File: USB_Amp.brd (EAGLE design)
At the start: 87 x 60 mm, 192 parts, among them CON1 AUDIO_IN, CON2 PROG, CON3 PWR IN, CON4 USB-C-2OZ, CON5 SWD, IC1 ISO7762, IC10 74LVC1G79, IC11 1.8V, IC12 AK1110, IC13 STM32G030F, IC14 CH221, IC15 7808, IC16 TAR5SB33, IC2 3.3V, IC3 PIC32MZEF, IC4 TAR5SB33, IC5 SSM3582, IC6 3G04, IC7 TL431, IC8 74LVC1G79, IC9 74LVC1G79, Q1 PNP, Q2 PNP, Q3 PNP, Q4 NPN, Q5 NPN, X1 12MHz, X2 22.5792MHz, X3 24.576MHz

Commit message: 微修正
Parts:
- added TP19, TP20: L_P, my_connector:TESTPIN-MID
- added TP21, TP22: R_N, my_connector:TESTPIN-MID
- L1, L2: value 7uH -> 7uH-UA8013
- R20: value LRCLK -> DATA
- R21: value DATA -> LRCLK
- moved C17 1.00 mm to (29.0, 25.4)
- moved C18 1.00 mm to (29.0, 34.6)
- moved C21 1.00 mm to (21.0, 25.4)
- moved C22 1.00 mm to (21.0, 34.6)
- moved C25 1.00 mm to (27.0, 23.8)
- moved C26 1.00 mm to (23.0, 23.8)
- moved C27 1.00 mm to (18.5, 29.0)
- moved C28 1.00 mm to (18.5, 31.0)
- moved C29 1.00 mm to (23.0, 36.2)
- moved C30 1.00 mm to (27.0, 36.2)
- moved C33 1.00 mm to (23.0, 37.5)
- moved C34 1.00 mm to (23.0, 22.5)
- moved C36 1.00 mm to (27.0, 37.5)
- moved C37 1.00 mm to (27.0, 22.5)
- moved C39 1.00 mm to (25.0, 22.0)
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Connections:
- net SPK_OUTN_L: now also TP19.1
- net SPK_OUTN_R: now also TP22.1
- net SPK_OUTP_L: now also TP20.1
- net SPK_OUTP_R: now also TP21.1
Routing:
- net GND: track 103.3 -> 98.6 mm, vias 773 -> 777
- net I2S_SCK_BUF: track 19.0 -> 20.0 mm
- net I2S_LRCLK_BUF: track 19.2 -> 20.2 mm
- net I2S_DATA_BUF: track 18.9 -> 19.9 mm
- net I2C_SDA: track 56.8 -> 57.8 mm
- net I2C_SCL: track 60.2 -> 61.2 mm
- net +8V: track 101.8 -> 102.8 mm
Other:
- board size 87 x 60 mm -> 88 x 60.1 mm

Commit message: v4.3
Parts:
- added D5, D6, D7, D8: SBD, my_rcl:SOD323
- added R42, R43: THJ, my_rcl:3216-2
- moved C46 1.03 mm to (35.0, 37.5)
- moved C47 1.03 mm to (35.0, 22.5)
- moved C1 1.00 mm to (84.2, 8.50)
- moved C10 1.00 mm to (65.8, 11.5)
- moved C11 1.00 mm to (65.8, 9.00)
- moved C12 1.00 mm to (74.2, 11.0)
- moved C13 1.00 mm to (71.5, 6.25)
- moved C14 1.00 mm to (78.5, 10.0)
- moved C15 1.00 mm to (77.8, 15.5)
- moved C16 1.00 mm to (52.5, 12.2)
- moved C17 1.00 mm to (30.0, 25.4)
- moved C18 1.00 mm to (30.0, 34.6)
- moved C19 1.00 mm to (57.2, 15.8)
- moved C2 1.00 mm to (82.0, 8.50)
- moved C20 1.00 mm to (51.2, 15.8)
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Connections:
- net AMP_OUTN_L: now also D5.2
- net AMP_OUTN_R: now also D8.2
- net AMP_OUTP_L: now also D6.2
- net AMP_OUTP_R: now also D7.2
- net DGND: now also R42.1, R43.1
- net GND: now also D5.1, D6.1, D7.1, D8.1, R42.2, R43.2
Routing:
- net GND: track 98.6 -> 95.0 mm, vias 777 -> 791
- net DGND: track 7.65 -> 9.61 mm, vias 112 -> 113
- net AMP_+5V: track 18.8 -> 19.9 mm
- added copper zone on layer 2, net GND4
- added copper zone on layer 1, net GND5
- added copper zone on layer 15, net GND5
- added copper zone on layer 16, net GND5
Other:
- board size 88 x 60.1 mm -> 88 x 60 mm
- board text added: "ver4.3"
- board text removed: "ver4.2"

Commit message: v6
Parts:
- removed D5, D6, D7, D8: SBD, my_rcl:SOD323
- removed FB6: FB, my_rcl:3216-FB
- added C89: 10n, my_rcl:3216
- added C90, C91: 0.1u, my_rcl:1005
- added IC17: 3.3V, my_ic:SOT23-5
- added R44: 1.5k, my_rcl:1608
- added R45, R46: THJ, my_rcl:1608-W
- added TP23: SDOUT, my_connector:TESTPAD-SMALL
- added TP24: G, my_connector:TESTPIN
- C1, C5: device my_rcl:2012 -> my_rcl:2012-POL
- C12: value 0.1u -> 2.2u; device my_rcl:1608C -> my_rcl:2012
- C13: value 1u -> 0.1u
- C14, C15: value 10p -> 0.1u; device my_rcl:1005 -> my_rcl:1608C
- C16: value 10u -> 0.1u; device my_rcl:2012-POL -> my_rcl:1608C
- C17, C18: value 0.22u -> 0.1u
- C19: value 2.2u -> 0.1u; device my_rcl:2012-POL -> my_rcl:1608C
- C2: value 1u -> 10u; device my_rcl:1608C -> my_rcl:2012
- C20: value 10u -> 0.1u; device my_rcl:2012-POL -> my_rcl:1005
- C21: value 0.22u -> 1u
- C22: value 0.22u -> 0.1u; device my_rcl:1608C -> my_rcl:1005
- C23: value 10u -> 1u; device my_rcl:2012 -> my_rcl:1005
- C24: value 2.2u -> 0.1u; device my_rcl:2012 -> my_rcl:1005
- C25, C26: value 10n -> 10p
- C27, C28, C7: device my_rcl:1608C -> my_rcl:1005
- C29: value 10n -> 1u; device my_rcl:1005 -> my_rcl:2012
- C3: value 0.1u -> 1u
- C30: value 10n -> 1u; device my_rcl:1005 -> my_rcl:1608C
- C31: value 0.1u -> 1u; device my_rcl:1608C -> my_rcl:2012
- C32: value 0.1u -> 0.47u
- C33: value 0.1u -> 1u; device my_rcl:1005 -> my_rcl:1608C
- C34, C35: value 0.1u -> 10u; device my_rcl:1005 -> my_rcl:3225
- C36: value 0.1u -> 0.47u; device my_rcl:1005 -> my_rcl:1608C
- C37: device my_rcl:1005 -> my_rcl:1608C
- C38: value 0.1u -> 25V 1000u; device my_rcl:1005 -> my_rcl:E5-10
- C39: value 1u -> 25V 1000u; device my_rcl:2012 -> my_rcl:E5-10
- C4: value 0.1u -> 2.2u; device my_rcl:1005 -> my_rcl:2012-POL
- C40: device my_rcl:2012 -> my_rcl:1608-W
- C42: value DNP -> 1u; device my_rcl:1608C -> my_rcl:3216-POL
- C43, C44: value 10u -> 0.1u; device my_rcl:3225 -> my_rcl:1005
- C45: value 0.1u -> 1u; device my_rcl:1005 -> my_rcl:2012
- C46: value 10u -> 1u; device my_rcl:3225 -> my_rcl:1608C
- C47: value 10u -> 1u; device my_rcl:3225 -> my_rcl:2012
- C48: value 4.7u -> 0.47u; device my_rcl:3216 -> my_rcl:1608C
- C49: value 16V 680u -> 1u; device my_rcl:E5-10 -> my_rcl:1608C
- C50: value 16V 680u -> 10u; device my_rcl:E5-10 -> my_rcl:3225
- C51: value 100p -> 1u
- C52: value 0.22u -> 10u; device my_rcl:C050W -> my_rcl:3225
- C53: value 100p -> 0.1u
- C54: value 16V 2200u -> 0.47u; device my_rcl:E5-13 -> my_rcl:1608C
- C55: value 1n -> 10u; device my_rcl:2012 -> my_rcl:3216
- C56: value 1n -> 1u; device my_rcl:2012 -> my_rcl:1608-W
- C57: value 10n -> 0.1u; device my_rcl:C050W2 -> my_rcl:1005
- C58: value 10n -> 1u; device my_rcl:C050W2 -> my_rcl:3216-POL
- C59: value 47u -> 0.1u; device my_rcl:E2.5-5 -> my_rcl:1608C
- C60: value 10u -> 100p; device my_rcl:2012 -> my_rcl:1608C
- C61: value 4.7u -> 100p; device my_rcl:2012 -> my_rcl:1608C
- C62: value 100u -> 22u; device my_rcl:E2.5-6.5 -> my_rcl:2012
- C63: value 0.1u -> DNP
- C65: value 0.22u -> 100p; device my_rcl:C050W -> my_rcl:1608C
- C66: value 100p -> 0.47u; device my_rcl:1608C -> my_rcl:C050W
- C67: value 1n -> 0.47u; device my_rcl:2012 -> my_rcl:C050W
- C68: value 1n -> 4.7u; device my_rcl:2012 -> my_rcl:3216
- C69: value 10u -> 1n
- C70: value 10n -> 1n; device my_rcl:C050W2 -> my_rcl:2012
- C71: value 10n -> 16V 680u; device my_rcl:C050W2 -> my_rcl:E5-10
- C72, C73: value 10u -> 10n; device my_rcl:2012 -> my_rcl:3216
- C74: value 0.1u -> 16V 680u; device my_rcl:1608C -> my_rcl:E5-10
- C76: value 25V 1000u -> 16V 2200u; device my_rcl:E5-10 -> my_rcl:E5-13
- C78: value 25V 1000u -> 100p; device my_rcl:E5-10 -> my_rcl:1608C
- C79: value 1u -> 100p
- C8, C9: value 0.1u -> 10u; device my_rcl:1608C -> my_rcl:2012
- C80: value 0.1u -> 100p
- C81: value 10u -> 100p; device my_rcl:3216 -> my_rcl:1608C
- C82: value 0.1u -> 0.47u; device my_rcl:1608C -> my_rcl:C050W
- C83: value 22u -> 0.47u; device my_rcl:2012 -> my_rcl:C050W
- C84: value 4.7u -> 10u
- C85: value 100p -> 10u; device my_rcl:1608C -> my_rcl:2012
- C86, C87: value 100p -> 1n; device my_rcl:1608C -> my_rcl:2012
- C88: value 100p -> 10n; device my_rcl:1608C -> my_rcl:3216
- FB4: device my_rcl:2012-R -> my_rcl:3216-FB
- IC1: value ISO7762 -> TAR5SB33; device my_ic:TSSOP16 -> my_ic:SOT23-5
- IC10: value 74LVC1G79 -> CH221; device my_ic:TSSOP5 -> my_ic:SOT23-6
- IC11: value 1.8V -> TAS5827; device my_ic:SOT23-5 -> my_ic:QFN32-TAS
- IC12: value AK1110 -> 7805; device my_ic:PLP10 -> my_ic:DPAK
- IC13: value STM32G030F -> TAR5SB33; device my_ic:TSSOP20 -> my_ic:SOT23-5
- IC14: value CH221 -> TL431; device my_ic:SOT23-6 -> my_ic:SC59
- IC15: value 7808 -> STM32G030F; device my_ic:DPAK -> my_ic:TSSOP20
- IC16: value TAR5SB33 -> 3.3V
- IC2: value 3.3V -> ISO7762; device my_ic:SOT23-5 -> my_ic:TSSOP16
- IC3: value PIC32MZEF -> 3.3V; device my_ic:QFN64HT -> my_ic:SOT23-5
- IC4: value TAR5SB33 -> 3G04; device my_ic:SOT23-5 -> my_ic:SSOP8-P-0.65
- IC5: value SSM3582 -> PIC32MZEF; device my_ic:QFN40HT -> my_ic:QFN64HT
- IC6: value 3G04 -> 74LVC1G79; device my_ic:SSOP8-P-0.65 -> my_ic:TSSOP5
- IC7: value TL431 -> 74LVC1G79; device my_ic:SC59 -> my_ic:TSSOP5
- IC9: value 74LVC1G79 -> TAS5827; device my_ic:TSSOP5 -> my_ic:QFN32-TAS
- R11: value 51 -> MCLK
- R12: value 39.2k -> MCLKB; device my_rcl:1608 -> my_rcl:1005
- R13: value 10k -> DATA; device my_rcl:1608 -> my_rcl:1005
- R14: value 1k -> LRCLK; device my_rcl:3216 -> my_rcl:1005
- R15: value 51 -> SCK; device my_rcl:2012 -> my_rcl:1005
- R16: value 51 -> 0; device my_rcl:2012 -> my_rcl:1005
- R17: value MCLK -> 5.1k; device my_rcl:1005 -> my_rcl:1608
- R18: value MCLKB -> 5.1k; device my_rcl:1005 -> my_rcl:1608
- R19: value SCK -> 200k; device my_rcl:1005 -> my_rcl:1608
- R20: value DATA -> 1k
- R21: value LRCLK -> 1k; device my_rcl:1005 -> my_rcl:2012
- R22: value 2.2 -> 100; device my_rcl:2012-R -> my_rcl:1608
- R23, R24: value 51 -> 10; device my_rcl:2012 -> my_rcl:1608
- R25, R26: value 3.3k -> 1k
- R27: value 50k -> 40.2k; device my_rcl:RK0972 -> my_rcl:1608
- R28: value DNP -> 10k
- R29: value 100k -> 3.3k
- R30: value 10k -> 3.3k
- R31: value 10k -> 50k; device my_rcl:1608 -> my_rcl:RK0972
- R32, R33: value 5.1k -> 5.1; device my_rcl:1608 -> my_rcl:2012
- R34: value 100k -> 1k; device my_rcl:1608 -> my_rcl:3216
- R35: value 10k -> DNP
- R36: value 1.5k -> 100k
- R37: value 1k -> 10k; device my_rcl:2012 -> my_rcl:1608
- R38: value 10 -> 10k
- R41: value 10 -> 5.1; device my_rcl:1608 -> my_rcl:2012
- R42: value THJ -> 5.1; device my_rcl:3216-2 -> my_rcl:2012
- R43: value THJ -> 10k; device my_rcl:3216-2 -> my_rcl:1608
- R7: value 100 -> THJ; device my_rcl:1608 -> my_rcl:3216-2
- R8: value 1k -> THJ; device my_rcl:1608 -> my_rcl:3216-2
- R9: value 1k -> 51; device my_rcl:1608 -> my_rcl:1005
- TP19: value L_P -> L_N
- TP22, TP4: value R_N -> R_P
- TP3: value R_P -> R_N
- X1: value 12MHz -> 22.5792MHz; device my_rcl:KC3225-CRYSTAL -> my_rcl:KC3225
- X2: value 22.5792MHz -> 24.576MHz
- X3: value 24.576MHz -> 12MHz; device my_rcl:KC3225 -> my_rcl:KC3225-CRYSTAL
- moved C62 74.0 mm to (80.0, 32.0), turned to 0 degrees
- moved C83 72.4 mm to (11.0, 54.0), turned to 180 degrees
- moved R42 69.3 mm to (13.5, 57.0), flipped to the bottom, turned to 225 degrees
- moved C82 67.0 mm to (11.0, 45.0), flipped to the top
- moved R33 66.7 mm to (11.0, 6.00), turned to 135 degrees
- moved R32 62.2 mm to (11.0, 15.0)
- moved C55 61.7 mm to (72.8, 35.8)
- moved C59 60.9 mm to (77.8, 39.8), flipped to the bottom, turned to 0 degrees
- moved FB4 59.1 mm to (70.0, 45.5), turned to 270 degrees
- moved IC12 58.1 mm to (70.0, 36.5), flipped to the bottom, turned to 270 degrees
- moved R38 56.2 mm to (77.0, 33.0), flipped to the top, turned to 270 degrees
- moved C51 54.6 mm to (60.0, 49.0), flipped to the top, turned to 270 degrees
- moved C26 54.4 mm to (77.8, 15.5), turned to 0 degrees
- moved C81 53.7 mm to (23.2, 56.2), turned to 180 degrees
- moved C21 53.1 mm to (71.5, 6.25), flipped to the bottom
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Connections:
- removed net +8V: C81.1, FB2.1, FB4.1, IC15.3, IC16.1, IC16.3
- removed net AMP_+5V: C61.1, C84.1, IC11.1, IC11.3, IC12.5
- removed net AMP_AVDD: C28.1, C59.+, C60.1, IC12.1, IC5.24
- removed net AMP_DVDD: C27.1, C69.1, IC11.5, IC5.28
- new net +5V: C55.1, FB1.1, IC12.3, IC13.1, IC13.3, IC16.1, IC16.3, IC17.1, IC17.3
- new net AMP_AVDD_L: C41.1, C42.1, IC9.19
- new net AMP_AVDD_R: C57.1, C58.1, IC11.19
- new net AMP_DVDD_L: C30.1, C84.1, IC16.5, IC9.6
- new net AMP_DVDD_R: C46.1, C85.1, IC11.6, IC17.5
- new net AMP_EN: IC11.17, IC15.20, IC9.17
- new net AMP_IO0: IC11.9, TP23.1
- new net N$47: IC11.8, R20.2
- new net N$48: C33.1, IC9.7
- new net N$49: C90.1, IC16.4
- new net N$50: C91.1, IC17.4
- net +12V: now also C27.1, C28.1, C31.1, C35.1, C45.1, C50.1, C52.1, C68.1, C71.+, C74.+, C76.+, IC11.21, IC11.22, IC11.3, IC11.4, IC9.21, IC9.22, IC9.3, IC9.4, R25.2, R27.2, R34.2; no longer C25.1, C26.1, C30.1, C33.1, C36.1, C37.1, C39.1, C40.1, C46.1, C48.1, C49.+, C50.+, C54.+, IC5.14, IC5.15, IC5.16, IC5.17, IC5.34, IC5.35, IC5.36, IC5.37, R12.2, R14.2, R8.2
- net +3V3: now also C62.1, C7.1, C75.1, IC13.5, IC15.4, IC2.16, R31.3, R31.6, R35.2, R37.2, R38.2; no longer C4.1, C74.1, C83.1, IC1.16, IC13.4, IC16.5, R27.3, R27.6, R28.2, R30.2, R31.2
- net +3V3A: now also C20.1, C22.1, C24.1, C8.1, IC4.8, IC6.5, IC7.5; no longer C35.1, C38.1, C41.1, C45.1, IC10.5, IC6.8, IC9.5
- net +3V3D: now also C14.1, C15.1, C18.1, C19.1, C21.1, IC2.1, IC3.5, IC5.19, IC5.26, IC5.34, IC5.39, IC5.54, IC5.60, IC5.8; no longer C12.1, C3.1, C5.1, C7.1, C8.1, IC1.1, IC2.5, IC3.19, IC3.26, IC3.34, IC3.39, IC3.54, IC3.60, IC3.8
- net AMP_OUTN_L: now also C36.1, IC9.30, R24.2; no longer C21.1, D5.2, IC5.32, IC5.33, R38.2
- net AMP_OUTN_R: now also C54.1, IC11.30, L2.1, R39.2; no longer C22.2, D8.2, IC5.18, IC5.19, L2.4, R40.2
- net AMP_OUTP_L: now also C32.1, IC9.2, R23.2; no longer C17.1, D6.2, IC5.38, IC5.39, R39.2
- net AMP_OUTP_R: now also C48.2, IC11.2, L2.4, R40.2; no longer C18.2, D7.2, IC5.12, IC5.13, L2.1, R41.2
- net DGND: now also C18.2, C19.2, C21.2, C25.2, C26.2, IC2.8, IC3.2, IC5.20, IC5.25, IC5.35, IC5.40, IC5.55, IC5.59, IC5.7, IC5.HT, IC5.HT2, R7.1, R8.1, X3.2, X3.4; no longer C1.2, C12.2, C5.2, C7.2, C8.2, IC1.8, IC2.2, IC3.20, IC3.25, IC3.35, IC3.40, IC3.55, IC3.59, IC3.7, IC3.HT, IC3.HT2, R42.1, R43.1, X1.2, X1.4
- net EN_441K: now also IC15.17, IC2.15, IC4.1, X1.1; no longer IC1.15, IC13.17, IC6.1, X2.1
- net EN_48K: now also IC4.7, X2.1; no longer IC6.7, X3.1
- net GND: now also C1.2, C12.2, C17.2, C22.2, C38.-, C39.-, C42.2, C49.2, C5.2, C50.2, C51.2, C52.2, C55.2, C57.2, C59.2, C62.2, C65.2, C66.1, C66.3, C67.2, C67.4, C69.1, C7.2, C70.2, C71.-, C72.1, C74.-, C78.2, C8.2, C80.1, C82.1, C82.3, C83.4, C86.1, C88.1, C89.2, C90.2, C91.2, IC1.2, IC10.2, IC11.20, IC11.25, IC11.26, IC11.31, IC11.32, IC11.5, IC11.HT, IC11.HT2, IC12.2, IC13.2, IC14.3, IC15.5, IC17.2, IC2.9, IC4.4, IC6.3, IC9.20, IC9.25, IC9.26, IC9.31, IC9.32, IC9.5, IC9.HT, IC9.HT2, R16.1, R17.2, R18.2, R20.1, R28.1, R30.1, R31.1, R31.4, R34.1, R36.1, R44.2, R45.1, R46.1, R7.2, R8.2, TP24.1, X1.2; no longer C19.2, C25.2, C26.2, C32.2, C36.2, C38.2, C39.2, C49.-, C50.-, C51.1, C54.-, C55.1, C57.1, C57.3, C58.4, C59.-, C62.-, C63.2, C66.2, C67.1, C68.2, C69.2, C70.1, C70.3, C71.2, C71.4, C72.2, C74.2, C78.-, C80.2, C82.2, C86.2, C88.2, D5.1, D6.1, D7.1, D8.1, IC1.9, IC10.3, IC11.2, IC12.10, IC12.6, IC12.8, IC12.HT, IC12.HT2, IC13.5, IC14.2, IC15.2, IC4.2, IC5.1, IC5.10, IC5.2, IC5.21, IC5.22, IC5.23, IC5.25, IC5.26, IC5.27, IC5.29, IC5.3, IC5.30, IC5.9, IC5.HT, IC5.HT2, IC6.4, IC9.3, R13.1, R14.1, R25.1, R26.1, R27.1, R27.4, R32.2, R33.2, R36.2, R42.2, R43.2, X3.2
- net I2C_SCL: now also IC11.16, IC15.1, IC9.16, R37.1; no longer IC13.1, IC5.4, R30.1
- net I2C_SDA: now also IC11.15, IC15.2, IC9.15, R38.1; no longer IC13.2, IC5.5, R31.1
- net I2S_DATA: now also IC6.1; no longer IC9.1
- net I2S_DATA_BUF: now also IC11.14, IC9.14, R13.2; no longer IC5.7, R20.2
- net I2S_LRCLK: now also IC15.7, IC7.1; no longer IC10.1, IC13.7
- net I2S_LRCLK_BUF: now also IC11.12, IC9.12, R14.2; no longer IC5.6, R21.2
- net I2S_MCLK: now also IC6.2, IC7.2, R9.2; no longer IC10.2, IC9.2, R10.2
- net I2S_MCLK2: now also IC4.3, R10.2; no longer IC6.3, R11.2
- net I2S_MCLK_BUF: now also IC2.11, R11.2, R12.2; no longer IC1.11, R17.2, R18.2
- net I2S_SCK_BUF: now also IC11.13, IC9.13, R15.2; no longer IC5.8, R19.2
- net LED0: now also IC15.8; no longer IC13.8
- net LED1: now also IC5.42; no longer IC3.42
- net MCLK_OSC: now also R9.1, X1.3; no longer R11.1, X3.3
- net MCLR: now also IC5.9; no longer IC3.9
- net N$10: now also IC6.4, R13.1; no longer IC8.4, R19.1
- net N$11: now also IC7.4, R14.1; no longer IC9.4, R20.1
- net N$12: now also C54.2, IC11.29; no longer C21.2, IC5.31
- net N$13: now also C32.2, IC9.1; no longer C17.2, IC5.40
- net N$14: now also IC8.4, R15.1; no longer IC10.4, R21.1
- net N$15: now also C73.1, R33.1; no longer C58.1, C58.3, R16.1
- net N$16: now also R25.1; no longer R8.1
- net N$17: now also C40.1, IC9.18; no longer C18.1, IC5.11
- net N$18: now also C36.2, IC9.29; no longer C22.1, IC5.20
- net N$19: now also C89.1, R42.1; no longer C71.1, C71.3, R24.1
- net N$20: now also C63.2, IC14.1, R26.1; no longer C42.2, IC7.1, R9.1
- net N$21: now also C88.2, R41.2; no longer C70.2, C70.4, R23.2
- net N$22: now also IC2.13; no longer IC1.13
- net N$23: now also C4.1, IC1.4; no longer C19.1, IC4.4
- net N$24: now also IC2.12; no longer IC1.12
- net N$25: now also C63.1, IC14.2; no longer C42.1, IC7.2
- net N$26: now also IC9.8, R16.2; no longer C73.1, IC12.7
- net N$27: now also C56.1, IC11.18; no longer C72.1, IC12.9
- net N$28: now also R22.1; no longer R7.1
- net N$29: now also C48.1, IC11.1; no longer C62.+, C63.1, IC12.2, IC12.3, IC12.4, R22.2
- net N$3: now also FB2.2; no longer FB1.2
- net N$30: now also C68.2, R26.2, R27.1, R28.2; no longer C48.2, R12.1, R13.2, R9.2
- net N$31: now also IC10.4, R17.1; no longer IC14.4, R32.1
- net N$32: now also IC10.5, R18.1; no longer IC14.5, R33.1
- net N$33: now also C51.1, IC10.1, R19.2, R21.1; no longer C79.1, IC14.1, R34.2, R37.1
- net N$34: now also IC10.6, R19.1; no longer IC14.6, R34.1
- net N$35: now also C59.1, IC13.4; no longer C82.1, IC16.4
- net N$36: now also R29.2; no longer R25.2
- net N$37: now also IC4.5, IC4.6, R12.1; no longer IC6.5, IC6.6, R18.1
- net N$39: now also IC4.2, R11.1; no longer IC6.2, R17.1
- net N$4: now also C3.1, IC3.1, IC3.3; no longer C1.1, IC2.1, IC2.3
- net N$40: now also C60.1, R23.1; no longer C86.1, R39.1
- net N$41: now also R30.2; no longer R26.2
- net N$42: now also C49.1, IC11.7; no longer FB4.2, R22.1
- net N$43: now also C1.1, FB1.2, IC1.1, IC1.3; no longer C16.1, FB2.2, IC4.1, IC4.3
- net N$44: now also C79.1; no longer C87.1
- net N$45: now also C61.1, R24.1; no longer C85.1, R38.1
- net N$46: now also C78.1, R39.1; no longer C88.1, R41.1
- net N$5: now also C25.1, IC5.31, X3.3; no longer C14.1, IC3.31, X1.3
- net N$6: now also C72.2, R32.2; no longer C57.2, C57.4, R15.2
- net N$7: now also C26.1, IC5.32, X3.1; no longer C15.1, IC3.32, X1.1
- net N$8: now also IC2.14; no longer IC1.14
- net PGEC: now also IC5.15; no longer IC3.15
- net PGED: now also IC5.16; no longer IC3.16
- net PIC_DATA: now also IC2.4, IC5.50; no longer IC1.4, IC3.50
- net PIC_DDC_EN: now also IC2.7; no longer IC1.7
- net PIC_EN441K: now also IC2.2, IC5.44; no longer IC1.2, IC3.44
- net PIC_LRCLK: now also IC2.5, IC5.52; no longer IC1.5, IC3.52
- net PIC_MCLK: now also IC2.6, IC5.57; no longer IC1.6, IC3.57
- net PIC_SCK: now also IC2.3, IC5.48, IC5.49; no longer IC1.3, IC3.48, IC3.49
- net SPK_OUTN_L: now also C65.1, C67.1, C67.3, C70.1, R33.2; no longer C52.2, C52.4, C53.1, C56.1, R16.2
- net SPK_OUTN_R: now also C80.2, C82.2, C82.4, C86.2, L2.2, R41.1, TP21.1, TP3.1; no longer C65.2, C65.4, C66.1, C68.1, L2.3, R24.2, TP22.1, TP4.1
- net SPK_OUTP_L: now also C64.2, C66.2, C66.4, C69.2, R32.1; no longer C51.2, C52.1, C52.3, C55.2, R15.1
- net SPK_OUTP_R: now also C81.1, C83.1, C83.3, C87.1, L2.3, R42.2, TP22.1, TP4.1; no longer C64.2, C65.1, C65.3, C67.2, L2.2, R23.1, TP21.1, TP3.1
- net STM_DDC_EN: now also IC15.16, IC2.10; no longer IC1.10, IC13.16
- net STM_TX: now also IC15.9; no longer IC13.9
- net SWCLK: now also IC15.19; no longer IC13.19
- net SWDIO: now also IC15.18; no longer IC13.18
- net UART_TX: now also IC5.1; no longer IC3.1
- net USB_D+: now also IC5.37; no longer IC3.37
- net USB_D-: now also IC5.36; no longer IC3.36
- net USB_VBUS: now also FB2.1, IC5.33; no longer FB1.1, IC3.33
- net V+: now also C37.1, C38.+, C39.+, C53.1, FB4.2, IC12.1, R22.2, R43.2, R45.2, R46.2; no longer C75.1, C76.+, C78.+, C80.1, FB6.2, IC15.1, R35.2, R7.2
- net V+_ADC: now also IC15.12, R43.1, R44.1; no longer IC13.12, R35.1, R36.1
- net VIN+: now also FB4.1; no longer FB5.1
- net VINC_+: now also FB5.1, R21.2; no longer FB6.1, R37.2
- net VOL_ADC: now also IC15.11, R31.2, R31.5, R35.1, R36.2; no longer IC13.11, R27.2, R27.5, R28.1, R29.2
- net XVCC: now also C12.1, C16.1, C17.1, C5.1, IC1.5, X1.4; no longer C20.1, C24.1, C31.1, C32.1, IC4.5, X3.4
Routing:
- net +5V: track 0.00 -> 117.5 mm, vias 0 -> 4
- net +8V: track 102.8 -> 0.00 mm
- net AMP_EN: track 0.00 -> 80.9 mm, vias 0 -> 3
- net GND: track 95.0 -> 41.6 mm, vias 791 -> 776
- net AMP_+5V: track 19.9 -> 0.00 mm
- net I2S_LRCLK_BUF: track 20.2 -> 32.8 mm, vias 0 -> 3
- net I2S_DATA_BUF: track 19.9 -> 32.5 mm, vias 0 -> 2
- net I2S_SCK_BUF: track 20.0 -> 32.5 mm
- net I2C_SDA: track 57.8 -> 69.3 mm, vias 2 -> 3
- net AMP_AVDD: track 10.6 -> 0.00 mm
- net AMP_DVDD: track 9.74 -> 0.00 mm
- net I2C_SCL: track 61.2 -> 70.6 mm, vias 2 -> 3
- net AMP_DVDD_R: track 0.00 -> 6.86 mm, vias 0 -> 1
- net AMP_DVDD_L: track 0.00 -> 6.55 mm, vias 0 -> 1
- net N$29: track 8.47 -> 2.37 mm
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- removed copper zone on layer 1, net AMP_+5V
- removed copper zone on layer 1, net AMP_AVDD
- removed copper zone on layer 1, net GND1
- removed copper zone on layer 15, net GND1
- removed copper zone on layer 16, net GND1
- removed copper zone on layer 2, net GND2
- removed copper zone on layer 1, net GND3
- removed copper zone on layer 15, net GND3
- removed copper zone on layer 16, net GND3
- removed copper zone on layer 1, net N$29
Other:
- board text added: "ver6"
- board text removed: "ver4.3"

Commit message: 発注
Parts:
- added C92, C93, C94, C95: 0.47u, my_rcl:1608C
- added R47: 47k, my_rcl:1608
- added TP25, TP26: AVDD, my_connector:TESTPIN-SMALL
- IC15: value STM32G030F -> STM32C011F
- R19: value 200k -> 100k
- R27: value 40.2k -> 39.2k
- R36: value 100k -> DNP
- moved R44 4.00 mm to (74.0, 43.8), turned to 0 degrees
- moved C84 1.90 mm to (30.0, 27.0), turned to 90 degrees
- moved C36 1.82 mm to (27.8, 18.5)
- moved C54 1.82 mm to (24.2, 43.5)
- moved R34 0.50 mm to (40.0, 16.0)
- moved C29 0.25 mm to (29.2, 23.8)
- moved C31 0.25 mm to (22.8, 23.8)
- moved C34 0.25 mm to (28.8, 21.0)
- moved C35 0.25 mm to (23.2, 21.0)
- moved C45 0.25 mm to (22.8, 38.2)
- moved C47 0.25 mm to (29.2, 38.2)
- moved C50 0.25 mm to (23.2, 41.0)
- moved C52 0.25 mm to (28.8, 41.0)
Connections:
- new net N$51: C92.2, IC9.28
- new net N$52: C93.2, IC9.24
- new net N$53: C94.1, IC11.24
- new net N$54: C95.2, IC11.28
- net AMP_AVDD_L: now also TP25.1
- net AMP_AVDD_R: now also TP26.1
- net AMP_EN: now also R47.2
- net AMP_OUTN_L: now also C92.1, C93.1, IC9.23, IC9.27; no longer C36.1, IC9.30
- net AMP_OUTN_R: now also C94.2, C95.1, IC11.23, IC11.27; no longer C54.1, IC11.30
- net AMP_OUTP_L: now also C36.1, IC9.30
- net AMP_OUTP_R: now also C54.1, IC11.30
- net GND: now also R47.1
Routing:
- net AMP_OUTN_R: track 2.26 -> 7.82 mm
- net AMP_OUTN_L: track 2.26 -> 7.82 mm
- net AMP_OUTP_R: track 4.33 -> 7.82 mm
- net AMP_OUTP_L: track 4.33 -> 7.82 mm
- net N$54: track 0.00 -> 2.95 mm
- net N$51: track 0.00 -> 2.95 mm
- net AMP_EN: track 80.9 -> 83.7 mm
- net N$53: track 0.00 -> 2.24 mm
- net N$52: track 0.00 -> 2.24 mm
- net +12V: track 41.4 -> 39.8 mm, vias 16 -> 18
- net V+_ADC: track 12.9 -> 11.4 mm
- net GND: vias 776 -> 779
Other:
- board text added: "ver6.1"
- board text removed: "ver6"

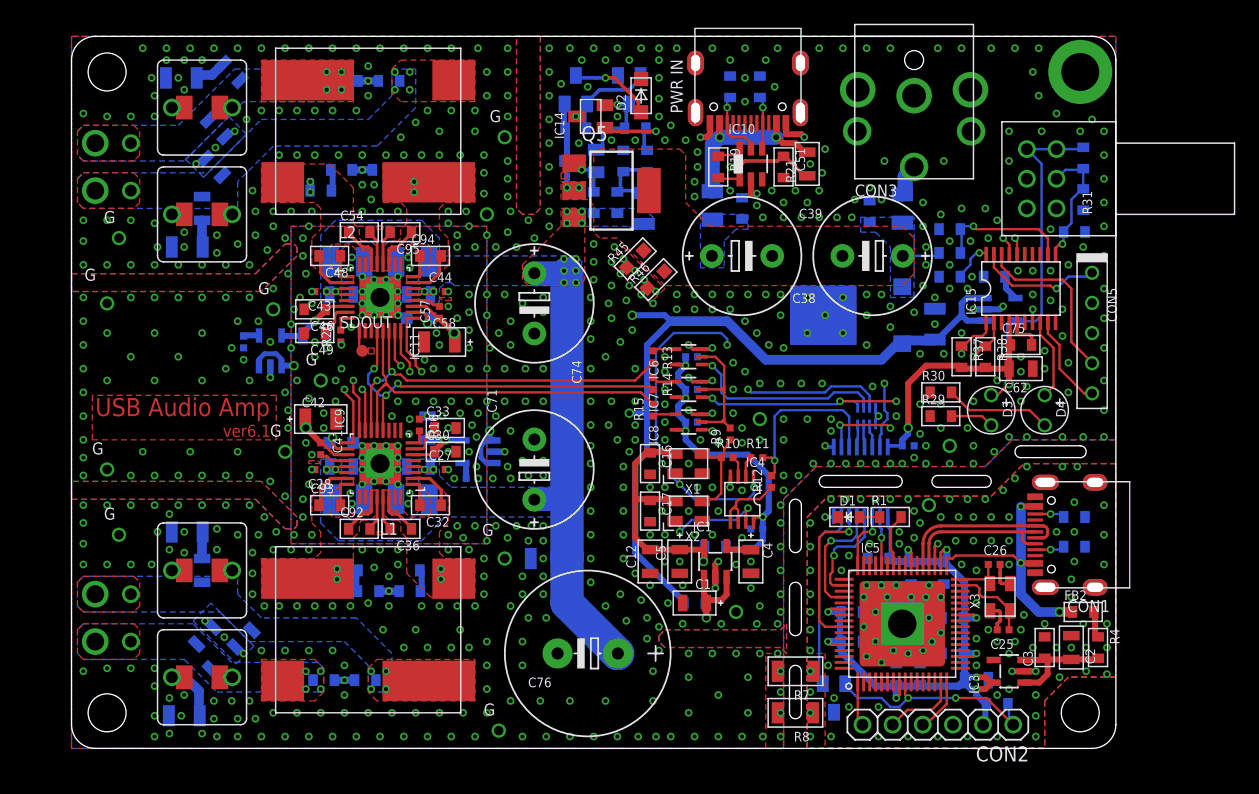
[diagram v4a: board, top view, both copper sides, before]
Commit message: FDA903D 発注
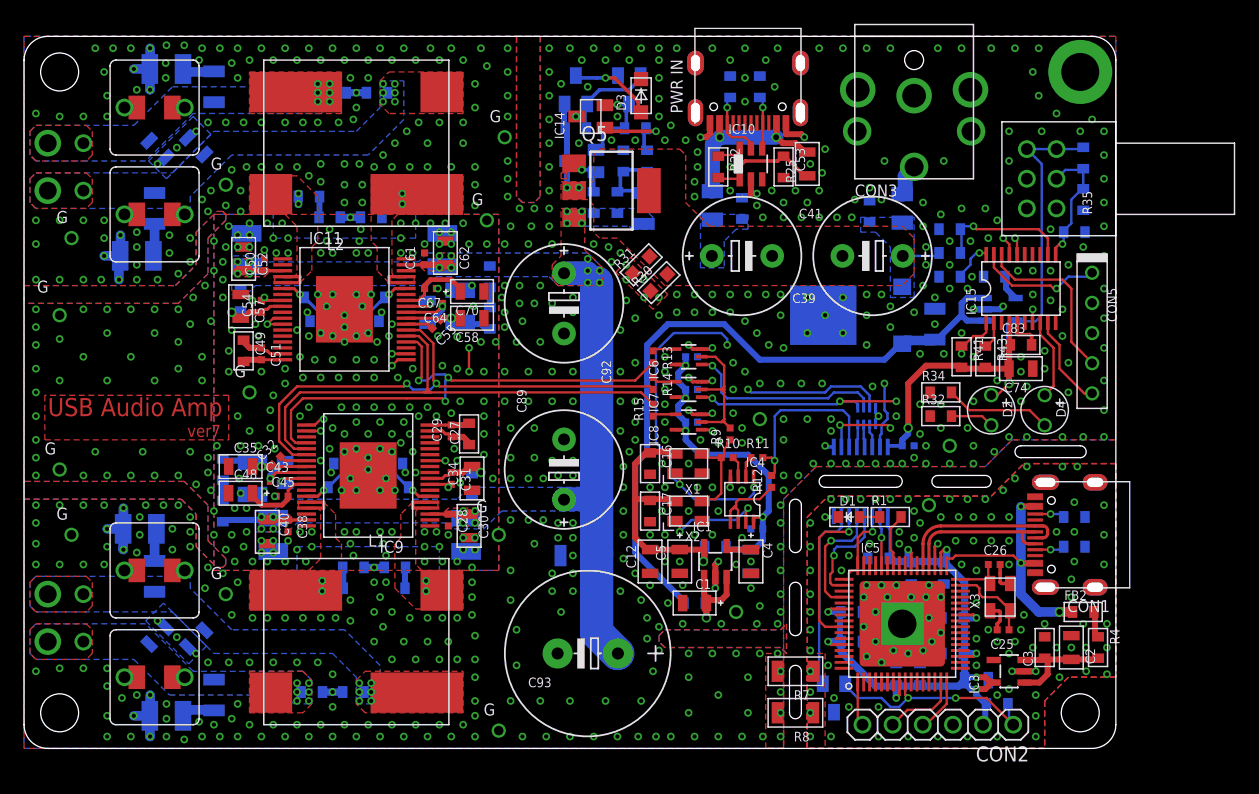
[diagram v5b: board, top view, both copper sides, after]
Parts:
- removed IC16, IC17: 3.3V, my_ic:SOT23-5
- removed TP23: SDOUT, my_connector:TESTPAD-SMALL
- removed TP25, TP26: AVDD, my_connector:TESTPIN-SMALL
- added C96, C97: 1n, my_rcl:2012
- added C98, C99: 0.22u, my_rcl:3225
- added FB6: FB, my_rcl:1608-FB
- added FB7: FB, my_rcl:3216-FB
- added R48: 47k, my_rcl:1608
- added R49: 1k, my_rcl:3216
- added R50, R51: 10, my_rcl:3216
- added R52: 10k, my_rcl:1608
- added R53: 1.5k, my_rcl:1608
- C27: value 0.1u -> 4.7u; device my_rcl:1005 -> my_rcl:1608C
- C29, C31, C45: value 1u -> 0.1u; device my_rcl:2012 -> my_rcl:1005
- C30: device my_rcl:1608C -> my_rcl:2012
- C32, C54: value 0.47u -> 0.1u; device my_rcl:1608C -> my_rcl:1005
- C33: value 1u -> 10u; device my_rcl:1608C -> my_rcl:3225
- C34, C35, C52: value 10u -> 1u; device my_rcl:3225 -> my_rcl:2012
- C36: value 0.47u -> 10u; device my_rcl:1608C -> my_rcl:3225-POL
- C38: value 25V 1000u -> 0.1u; device my_rcl:E5-10 -> my_rcl:1005
- C40: device my_rcl:1608-W -> my_rcl:2012
- C41: value 0.1u -> 25V 1000u; device my_rcl:1005 -> my_rcl:E5-10
- C42: value 1u -> 10u; device my_rcl:3216-POL -> my_rcl:3225
- C44: value 0.1u -> 4.7u; device my_rcl:1005 -> my_rcl:2012-POL
- C46: value 1u -> DNP
- C47: value 1u -> DNP; device my_rcl:2012 -> my_rcl:1608C
- C48: value 0.47u -> 4.7u; device my_rcl:1608C -> my_rcl:2012-POL
- C49: value 1u -> 4.7u
- C50: value 10u -> 0.1u; device my_rcl:3225 -> my_rcl:1005
- C51: value 1u -> 0.1u; device my_rcl:1608C -> my_rcl:1005
- C53: value 0.1u -> 1u
- C55: value 10u -> 0.1u; device my_rcl:3216 -> my_rcl:1005
- C56: value 1u -> 10u; device my_rcl:1608-W -> my_rcl:3225
- C57: value 0.1u -> 1u; device my_rcl:1005 -> my_rcl:2012
- C58: device my_rcl:3216-POL -> my_rcl:2012
- C60: value 100p -> 10u; device my_rcl:1608C -> my_rcl:3225-POL
- C61, C64: value 100p -> 0.1u; device my_rcl:1608C -> my_rcl:1005
- C62: value 22u -> 1u
- C63: value DNP -> 10u; device my_rcl:1608C -> my_rcl:3225
- C65: value 100p -> 10u; device my_rcl:1608C -> my_rcl:3216
- C66: value 0.47u -> 4.7u; device my_rcl:C050W -> my_rcl:2012-POL
- C67: value 0.47u -> 0.1u; device my_rcl:C050W -> my_rcl:1005
- C68: value 4.7u -> DNP; device my_rcl:3216 -> my_rcl:1608C
- C69: value 1n -> DNP; device my_rcl:2012 -> my_rcl:1608C
- C70: value 1n -> 4.7u; device my_rcl:2012 -> my_rcl:2012-POL
- C71: value 16V 680u -> 0.1u; device my_rcl:E5-10 -> my_rcl:1608C
- C72, C73: value 10n -> 470p; device my_rcl:3216 -> my_rcl:1608C
- C74: value 16V 680u -> 22u; device my_rcl:E5-10 -> my_rcl:2012
- C75: value 0.1u -> 100p
- C76: value 16V 2200u -> 100p; device my_rcl:E5-13 -> my_rcl:1608C
- C77: value 1n -> 0.47u; device my_rcl:1608C -> my_rcl:C050W
- C78: value 100p -> 0.47u; device my_rcl:1608C -> my_rcl:C050W
- C79, C80: value 100p -> 1n; device my_rcl:1608C -> my_rcl:2012
- C81: value 100p -> 0.22u; device my_rcl:1608C -> my_rcl:3225
- C82: value 0.47u -> 0.22u; device my_rcl:C050W -> my_rcl:3225
- C83: value 0.47u -> 0.1u; device my_rcl:C050W -> my_rcl:1608C
- C84: value 10u -> DNP; device my_rcl:2012 -> my_rcl:1608C
- C85: value 10u -> 1n; device my_rcl:2012 -> my_rcl:1608C
- C86, C87: value 1n -> 470p; device my_rcl:2012 -> my_rcl:1608C
- C88: value 10n -> 4.7u
- C89: value 10n -> 16V 680u; device my_rcl:3216 -> my_rcl:E5-10
- C90, C91: value 0.1u -> 100p; device my_rcl:1005 -> my_rcl:1608C
- C92: value 0.47u -> 16V 680u; device my_rcl:1608C -> my_rcl:E5-10
- C93: value 0.47u -> 16V 2200u; device my_rcl:1608C -> my_rcl:E5-13
- C94, C95: device my_rcl:1608C -> my_rcl:C050W
- D2: value 1mA -> PWR; device my_rcl:SOD123 -> my_rcl:LED2.5
- D3: value PWR -> 1mA; device my_rcl:LED2.5 -> my_rcl:SOD123
- FB4: device my_rcl:3216-FB -> my_rcl:1608-FB
- IC11, IC9: value TAS5827 -> FDA903D; device my_ic:QFN32-TAS -> my_ic:POWER-SSO36
- L1, L2: value 7uH-UA8013 -> 10uH-UA8014
- R16: value 0 -> 10; device my_rcl:1005 -> my_rcl:1608
- R17: value 5.1k -> 10
- R18: value 5.1k -> 0
- R19: value 100k -> 0
- R20: value 1k -> 5.1k; device my_rcl:1005 -> my_rcl:1608
- R21: value 1k -> 5.1k; device my_rcl:2012 -> my_rcl:1608
- R22: value 100 -> 100k
- R25: device my_rcl:1608 -> my_rcl:2012
- R26: value 1k -> 0
- R27: value 39.2k -> 0
- R28: value 10k -> 10
- R29: value 3.3k -> 10
- R30: value 3.3k -> THJ; device my_rcl:1608 -> my_rcl:1608-W
- R31: value 50k -> THJ; device my_rcl:RK0972 -> my_rcl:1608-W
- R32: value 5.1 -> 3.3k; device my_rcl:2012 -> my_rcl:1608
- R33: value 5.1 -> 100; device my_rcl:2012 -> my_rcl:1608
- R34: value 1k -> 3.3k; device my_rcl:3216 -> my_rcl:1608
- R35: value DNP -> 50k; device my_rcl:1608 -> my_rcl:RK0972
- R36: value DNP -> 10; device my_rcl:1608 -> my_rcl:3216
- R37: value 10k -> 10; device my_rcl:1608 -> my_rcl:3216
- R38: value 10k -> DNP
- R39: value 10 -> DNP
- R40: value 10 -> 1k
- R41: value 5.1 -> 10k; device my_rcl:2012 -> my_rcl:1608
- R42: value 5.1 -> 1k; device my_rcl:2012 -> my_rcl:1608
- R44: value 1.5k -> 39.2k
- R45: value THJ -> 10k; device my_rcl:1608-W -> my_rcl:1608
- R46: value THJ -> 10; device my_rcl:1608-W -> my_rcl:1608
- R47: value 47k -> 10
- TP1, TP20: value L_P -> L_N
- TP19, TP2: value L_N -> L_P
- TP21, TP3: value R_N -> R_P
- TP22, TP4: value R_P -> R_N
- X1: value 22.5792MHz -> 22.5792M
- X2: value 24.576MHz -> 24.576M
- moved R36 84.4 mm to (7.00, 14.5)
- moved C77 82.6 mm to (7.00, 15.0), flipped to the top, turned to 0 degrees
- moved C83 71.8 mm to (80.0, 34.0), turned to 0 degrees
- moved R37 69.1 mm to (12.0, 4.50), flipped to the bottom, turned to 90 degrees
- moved R41 65.2 mm to (75.0, 33.0), flipped to the top
- moved C85 64.6 mm to (84.5, 43.5)
- moved R32 63.6 mm to (73.2, 28.0), flipped to the top, turned to 0 degrees
- moved C75 63.4 mm to (23.8, 4.75), flipped to the bottom, turned to 180 degrees
- moved FB4 61.3 mm to (12.8, 23.5), turned to 90 degrees
- moved C65 59.6 mm to (72.8, 35.8), turned to 90 degrees
- moved R39 57.3 mm to (85.2, 46.2), turned to 90 degrees
- moved R33 56.0 mm to (42.5, 52.2), turned to 0 degrees
- moved R47 54.4 mm to (20.0, 46.5), turned to 0 degrees
- moved C38 54.3 mm to (18.2, 18.8), turned to 270 degrees
- moved R29 53.3 mm to (22.0, 13.5), flipped to the bottom
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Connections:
- removed net AMP_IO0: IC11.9, TP23.1
- removed net N$12: C54.2, IC11.29
- removed net N$13: C32.2, IC9.1
- removed net N$17: C40.1, IC9.18
- removed net N$18: C36.2, IC9.29
- removed net N$26: IC9.8, R16.2
- removed net N$29: C48.1, IC11.1
- removed net N$42: C49.1, IC11.7
- removed net N$47: IC11.8, R20.2
- removed net N$48: C33.1, IC9.7
- removed net N$49: C90.1, IC16.4
- removed net N$51: C92.2, IC9.28
- removed net N$52: C93.2, IC9.24
- removed net N$53: C94.1, IC11.24
- removed net N$54: C95.2, IC11.28
- new net AMP_1V8_L: C27.1, C29.1, IC9.17
- new net AMP_1V8_R: C49.1, C51.1, IC11.17
- new net AMP_5V_L: C43.1, C44.1, IC9.27
- new net AMP_5V_R: C64.1, C66.1, IC11.27
- new net AMP_AVSS_L: C43.2, C44.2, IC9.28
- new net AMP_AVSS_R: C64.2, C66.2, IC11.28
- new net AMP_DVSS_L: C27.2, C29.2, IC9.18
- new net AMP_DVSS_R: C49.2, C51.2, IC11.18
- new net AMP_FBN_L: C47.1, IC9.6, R19.2
- new net AMP_FBN_R: C69.1, IC11.6, R27.2
- new net AMP_FBP_L: C46.1, IC9.31, R18.2
- new net AMP_FBP_R: C68.1, IC11.31, R26.2
- new net AMP_SVR_L: C45.2, C48.1, IC9.29
- new net AMP_SVR_R: C67.2, C70.1, IC11.29
- net +12V: now also C30.1, C33.1, C38.1, C40.1, C42.1, C56.1, C61.1, C62.1, C63.1, C88.1, C89.+, C92.+, C93.+, IC11.35, IC9.35, R16.1, R17.1, R23.1, R24.1, R40.2, R44.2, R49.2; no longer C27.1, C29.1, C31.1, C34.1, C35.1, C43.1, C44.1, C45.1, C47.1, C68.1, C71.+, C74.+, C76.+, IC11.21, IC11.22, IC11.4, IC9.21, IC9.22, IC9.4, R25.2, R27.2, R34.2
- net +3V3: now also C74.1, C83.1, D2.A, R35.3, R35.6, R41.2, R43.2; no longer C62.1, C75.1, D3.A, R31.3, R31.6, R35.2, R37.2
- net +5V: now also C65.1; no longer C55.1, IC16.1, IC16.3, IC17.1, IC17.3
- net AMP_AVDD_L: now also C32.1, C35.1, C36.1, FB4.2, IC9.26; no longer C41.1, C42.1, IC9.19, TP25.1
- net AMP_AVDD_R: now also C55.1, C60.1, FB6.2, IC11.26; no longer C57.1, IC11.19, TP26.1
- net AMP_DVDD_L: now also C31.1, C34.1, IC9.9, R17.2; no longer C30.1, C84.1, IC16.5, IC9.6
- net AMP_DVDD_R: now also C54.1, C57.1, IC11.9, R24.2; no longer C46.1, C85.1, IC11.6, IC17.5
- net AMP_EN: now also IC11.11, IC11.12, IC9.12, R48.2; no longer IC11.17, IC9.17, R47.2
- net AMP_OUTN_L: now also IC9.4, IC9.5, L1.4, R28.2; no longer C92.1, C93.1, IC9.23, IC9.27, L1.1, R24.2
- net AMP_OUTN_R: now also IC11.4, IC11.5, L2.4, R47.2; no longer C94.2, C95.1, IC11.23, IC11.27, L2.1, R39.2
- net AMP_OUTP_L: now also IC9.32, IC9.33, L1.1, R29.2; no longer C32.1, C36.1, IC9.2, IC9.30, L1.4, R23.2
- net AMP_OUTP_R: now also IC11.32, IC11.33, L2.1, R46.2; no longer C48.2, C54.1, IC11.2, IC11.30, L2.4, R40.2
- net GND: now also C32.2, C36.2, C38.2, C41.-, C45.1, C48.2, C54.2, C63.2, C67.1, C68.2, C69.2, C71.2, C72.2, C74.2, C75.1, C76.2, C77.1, C77.3, C78.4, C79.1, C80.2, C81.1, C82.2, C86.2, C89.-, C90.1, C92.-, C93.-, C94.1, C94.3, C95.2, C95.4, C96.1, C97.2, C98.1, C99.2, D3.2, IC11.1, IC11.10, IC11.13, IC11.2, IC11.36, IC11.8, IC9.1, IC9.10, IC9.11, IC9.13, IC9.2, IC9.36, IC9.8, R20.2, R21.2, R32.1, R35.1, R35.4, R39.1, R48.1, R49.1, R53.2; no longer C27.2, C29.2, C38.-, C41.2, C43.2, C44.2, C45.2, C49.2, C51.2, C64.1, C66.1, C66.3, C67.2, C67.4, C69.1, C71.-, C72.1, C74.-, C75.2, C76.-, C77.2, C79.2, C80.1, C81.2, C82.1, C82.3, C83.4, C84.2, C86.1, C88.1, C89.2, C90.2, D2.2, IC11.20, IC11.26, IC11.31, IC11.32, IC11.5, IC11.HT2, IC16.2, IC17.2, IC9.20, IC9.26, IC9.31, IC9.32, IC9.5, IC9.HT2, R16.1, R17.2, R18.2, R20.1, R28.1, R29.1, R31.4, R36.1, R44.2, R46.1, R47.1
- net I2C_SCL: now also IC11.20, IC9.20, R41.1; no longer IC11.16, IC9.16, R37.1
- net I2C_SDA: now also IC11.19, IC9.19, R43.1; no longer IC11.15, IC9.15, R38.1
- net I2S_DATA_BUF: now also IC11.22, IC9.22; no longer IC11.14, IC9.14
- net I2S_LRCLK_BUF: now also IC11.24, IC9.24; no longer IC11.12, IC9.12
- net I2S_SCK_BUF: now also IC11.23, IC9.23; no longer IC11.13, IC9.13
- net N$15: now also C82.1, R37.1; no longer C73.1, R33.1
- net N$16: now also R40.1; no longer R25.1
- net N$19: now also C99.1, R51.1; no longer C89.1, R42.1
- net N$20: now also C84.2, R42.1; no longer C63.2, R26.1
- net N$21: now also C98.2, R50.2; no longer C88.2, R41.2
- net N$25: now also C84.1; no longer C63.1
- net N$27: now also FB6.1, R23.2; no longer C56.1, IC11.18
- net N$28: now also R33.1; no longer R22.1
- net N$30: now also C88.2, R42.2, R44.1, R45.2; no longer C68.2, R26.2, R27.1, R28.2
- net N$31: now also R20.1; no longer R17.1
- net N$32: now also R21.1; no longer R18.1
- net N$33: now also C53.1, R22.2, R25.1; no longer C51.1, R19.2, R21.1
- net N$34: now also R22.1; no longer R19.1
- net N$35: now also C71.1; no longer C59.1
- net N$36: now also D2.K, R32.2; no longer D3.K, R29.2
- net N$38: now also D3.1; no longer D2.1
- net N$40: now also C72.1, R28.1; no longer C60.1, R23.1
- net N$41: now also R34.2; no longer R30.2
- net N$44: now also C87.1, R47.1; no longer C79.1, R40.1
- net N$45: now also C73.1, R29.1; no longer C61.1, R24.1
- net N$46: now also C86.1, R46.1; no longer C78.1, R39.1
- net N$50: now also FB4.1, R16.2; no longer C91.1, IC17.4
- net N$6: now also C81.2, R36.2; no longer C72.2, R32.2
- net SPK_OUTN_L: now also C75.2, C77.2, C77.4, C79.2, L1.3, R19.1, R36.1, TP1.1, TP20.1; no longer C65.1, C67.1, C67.3, C70.1, L1.2, R33.2, TP19.1, TP2.1
- net SPK_OUTN_R: now also C91.1, C95.1, C95.3, C97.1, L2.3, R27.1, R51.2, TP22.1, TP4.1; no longer C80.2, C82.2, C82.4, C86.2, L2.2, R41.1, TP21.1, TP3.1
- net SPK_OUTP_L: now also C76.1, C78.1, C78.3, C80.1, L1.2, R18.1, R37.2, TP19.1, TP2.1; no longer C64.2, C66.2, C66.4, C69.2, L1.3, R32.1, TP1.1, TP20.1
- net SPK_OUTP_R: now also C90.2, C94.2, C94.4, C96.2, L2.2, R26.1, R50.1, TP21.1, TP3.1; no longer C81.1, C83.1, C83.3, C87.1, L2.3, R42.2, TP22.1, TP4.1
- net V+: now also C41.+, C59.1, FB7.2, R30.2, R31.2, R33.2, R52.2; no longer C38.+, C53.1, FB4.2, R22.2, R43.2, R45.2, R46.2
- net V+_ADC: now also R52.1, R53.1; no longer R43.1, R44.1
- net VIN+: now also FB5.1; no longer FB4.1
- net VINC_+: now also FB7.1, R25.2; no longer FB5.1, R21.2
- net VOL_ADC: now also C85.1, R35.2, R35.5, R38.1, R39.2; no longer C77.1, R31.2, R31.5, R35.1, R36.2
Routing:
- net +5V: track 117.5 -> 59.2 mm, vias 4 -> 0
- net SPK_OUTP_L: track 1.04 -> 26.0 mm, vias 4 -> 7
- net SPK_OUTP_R: track 1.04 -> 25.1 mm, vias 4 -> 7
- net SPK_OUTN_R: track 1.04 -> 22.8 mm, vias 4 -> 7
- net SPK_OUTN_L: track 1.04 -> 22.8 mm, vias 4 -> 7
- net GND: track 41.6 -> 62.8 mm, vias 779 -> 877
- net +12V: track 39.8 -> 55.9 mm, vias 18 -> 25
- net I2S_DATA_BUF: track 32.5 -> 44.7 mm, vias 2 -> 3
- net I2S_LRCLK_BUF: track 32.8 -> 45.0 mm, vias 3 -> 2
- net I2S_SCK_BUF: track 32.5 -> 43.6 mm
- net AMP_EN: track 83.7 -> 90.8 mm, vias 3 -> 5
- net AMP_SVR_R: track 0.00 -> 6.27 mm
- net AMP_SVR_L: track 0.00 -> 6.27 mm
- net AMP_5V_R: track 0.00 -> 5.52 mm, vias 0 -> 1
- net AMP_5V_L: track 0.00 -> 5.52 mm, vias 0 -> 1
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- added copper zone on layer 2, net SPK_OUTN_L
- added copper zone on layer 2, net SPK_OUTN_R
- added copper zone on layer 2, net SPK_OUTP_L
- added copper zone on layer 2, net SPK_OUTP_R
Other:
- board size 88 x 60 mm -> 92 x 60 mm
- board text added: "ver7"
- board text removed: "ver6.1"
